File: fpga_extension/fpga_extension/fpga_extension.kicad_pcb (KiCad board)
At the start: 4 copper layers, 50 x 34.7 mm, 78 parts, among them J1 Conn_02x16_Odd_Even, U1 AMS1117-1.2, U2 t20f169, U501 W9825G6KH-6, X1 SG-8101CG, X2 SG-8101CG

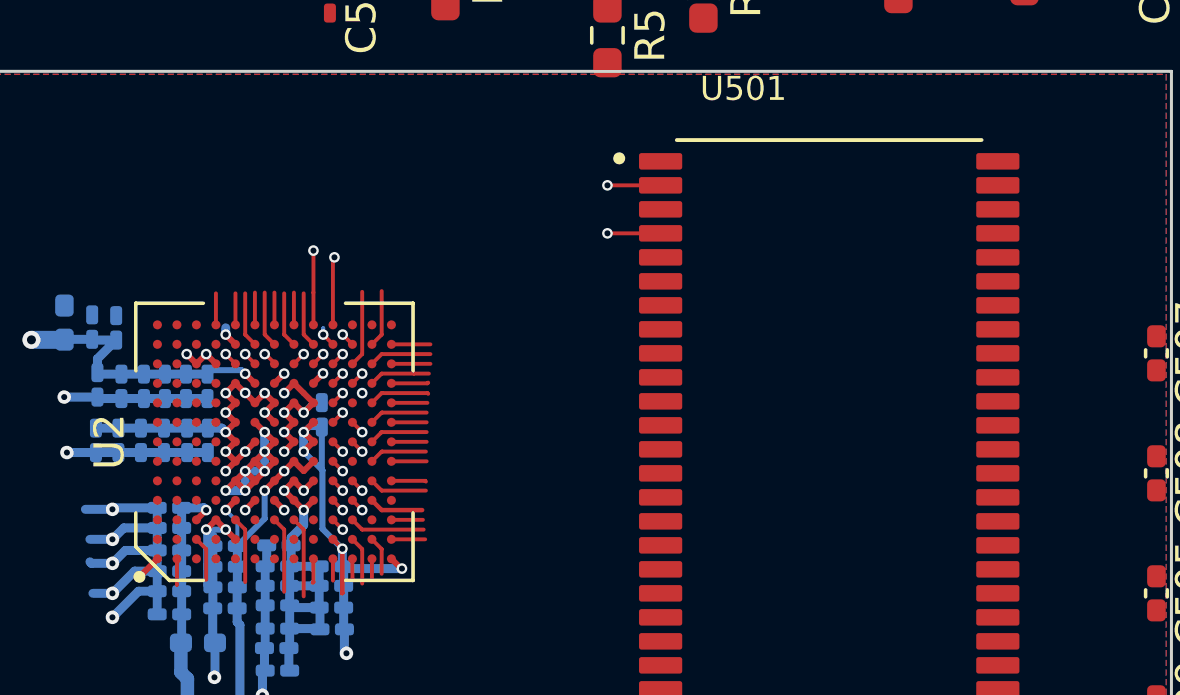
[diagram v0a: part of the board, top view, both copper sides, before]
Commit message: working on new version of fpga extension with Lattice FPGA
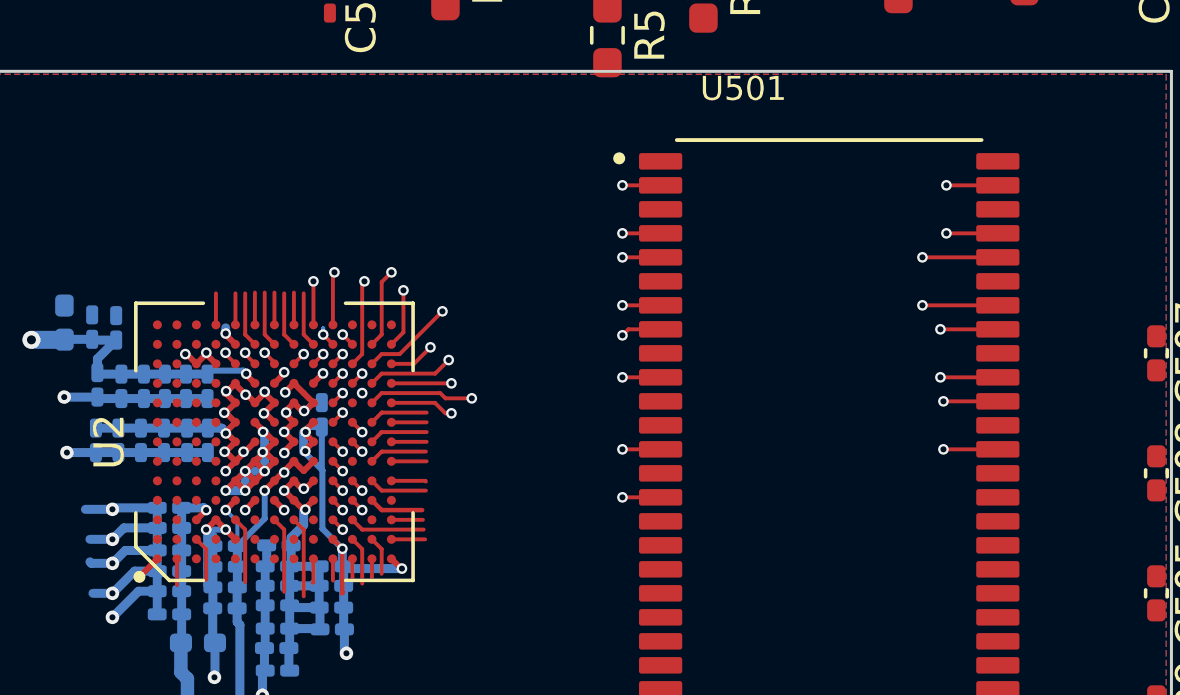
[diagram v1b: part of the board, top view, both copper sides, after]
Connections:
- U2 pad K10: /SDRAM/RAM_D8 -> /SDRAM/RAM_D12
- U2 pad K11: /SDRAM/RAM_D6 -> /SDRAM/RAM_D13
- U2 pad L10: /SDRAM/RAM_CS# -> /SDRAM/RAM_D3
- U2 pad L11: /SDRAM/RAM_RAS# -> /SDRAM/RAM_D15
- U2 pad M10: /SDRAM/RAM_CAS# -> /SDRAM/RAM_D5
- U2 pad M11: /SDRAM/RAM_D5 -> /SDRAM/RAM_D4
- U2 pad M12: /SDRAM/RAM_BS1 -> /SDRAM/RAM_D14
- U2 pad N10: /SDRAM/RAM_D7 -> /SDRAM/RAM_D10
- U2 pad N11: /SDRAM/RAM_D4 -> /SDRAM/RAM_D11
- U2 pad N12: /SDRAM/RAM_BS0 -> /SDRAM/RAM_D2
- U2 pad N2: /SDRAM/RAM_D2 -> /SDRAM/RAM_A3
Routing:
- net /SDRAM/RAM_D14: track 2.56 -> 33.5 mm, vias 1 -> 3
- net /SDRAM/RAM_D3: track 0.00 -> 29.1 mm, vias 0 -> 1
- net /SDRAM/RAM_D2: track 1.12 -> 28.5 mm, vias 0 -> 2
- net /SDRAM/RAM_D4: track 1.30 -> 28.6 mm, vias 0 -> 3
- net /SDRAM/RAM_D5: track 2.08 -> 28.5 mm, vias 0 -> 2
- net /SDRAM/RAM_D15: track 0.00 -> 26.2 mm, vias 0 -> 2
- net /SDRAM/RAM_D13: track 1.18 -> 27.3 mm, vias 0 -> 2
- net /SDRAM/RAM_LDQM: track 3.33 -> 29.4 mm, vias 1 -> 3
- net /SDRAM/RAM_D12: track 2.61 -> 26.8 mm, vias 1 -> 3
- net /SDRAM/RAM_D9: track 2.02 -> 26.1 mm, vias 0 -> 2
- net /SDRAM/RAM_D10: track 3.60 -> 26.1 mm, vias 1 -> 2
- net /SDRAM/RAM_D11: track 1.96 -> 23.8 mm, vias 0 -> 2
- net /SDRAM/RAM_D1: track 14.2 -> 29.1 mm
- net /SDRAM/RAM_D0: track 17.5 -> 31.0 mm
- net /SDRAM/RAM_D8: track 3.68 -> 0.00 mm
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
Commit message: prepared first versions of PCBs
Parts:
- removed C101, C102, C201, C202, C501, C505: 4.7u, Capacitor_SMD:C_0402_1005Metric_Pad0.74x0.62mm_HandSolder
- removed C103, C203, C502, C503, C504: 0.1u, Capacitor_SMD:C_0201_0603Metric_Pad0.64x0.40mm_HandSolder
- removed C506, C507, C508, C509: 0.1u, Capacitor_SMD:C_0402_1005Metric_Pad0.74x0.62mm_HandSolder
- removed L101, L201, L501: 33ohm 100MHz, Inductor_SMD:L_0402_1005Metric_Pad0.77x0.64mm_HandSolder
- removed R101, R201: 33R, Resistor_SMD:R_0603_1608Metric_Pad0.98x0.95mm_HandSolder
- removed R301: 50R, Resistor_SMD:R_0603_1608Metric_Pad0.98x0.95mm_HandSolder
- removed U501: W9825G6KH-6, ram:SOP80P1176X120-54N
- removed X2: SG-8101CG, Oscillator:Oscillator_SMD_SeikoEpson_SG210-4Pin_2.5x2.0mm_HandSoldering
- added C3: 100n, Capacitor_SMD:C_0402_1005Metric_Pad0.74x0.62mm_HandSolder, B.Cu at (159.0, 93.1)
- added C45: 100n, Capacitor_SMD:C_0402_1005Metric_Pad0.74x0.62mm_HandSolder, B.Cu at (152.2, 97.5)
- added C46: 100n, Capacitor_SMD:C_0402_1005Metric_Pad0.74x0.62mm_HandSolder, B.Cu at (155.2, 97.6)
- added C47: 100n, Capacitor_SMD:C_0402_1005Metric_Pad0.74x0.62mm_HandSolder, B.Cu at (148.7, 93.9)
- added C48: 100n, Capacitor_SMD:C_0402_1005Metric_Pad0.74x0.62mm_HandSolder, B.Cu at (148.7, 92.8)
- added C49: 100n, Capacitor_SMD:C_0402_1005Metric_Pad0.74x0.62mm_HandSolder, B.Cu at (148.7, 91.7)
- added C50: 100n, Capacitor_SMD:C_0402_1005Metric_Pad0.74x0.62mm_HandSolder, B.Cu at (154.8, 88.5)
- added C51: 100n, Capacitor_SMD:C_0402_1005Metric_Pad0.74x0.62mm_HandSolder, B.Cu at (152.6, 88.5)
- added C52: 100n, Capacitor_SMD:C_0402_1005Metric_Pad0.74x0.62mm_HandSolder, F.Cu at (180.2, 84.7)
- added C53: 100n, Capacitor_SMD:C_0402_1005Metric_Pad0.74x0.62mm_HandSolder, B.Cu at (159.0, 89.9)
- added C54: 100n, Capacitor_SMD:C_0402_1005Metric_Pad0.74x0.62mm_HandSolder, B.Cu at (159.0, 91.0)
- added C55: 100n, Capacitor_SMD:C_0402_1005Metric_Pad0.74x0.62mm_HandSolder, B.Cu at (158.9, 92.0)
- added C56: 100n, Capacitor_SMD:C_0402_1005Metric_Pad0.74x0.62mm_HandSolder, B.Cu at (150.3, 88.5)
- added C57: 100n, Capacitor_SMD:C_0402_1005Metric_Pad0.74x0.62mm_HandSolder, B.Cu at (149.7, 96.8)
- added C58: 100n, Capacitor_SMD:C_0402_1005Metric_Pad0.74x0.62mm_HandSolder, B.Cu at (157.2, 96.3)
- added C59: 100n, Capacitor_SMD:C_0402_1005Metric_Pad0.74x0.62mm_HandSolder, B.Cu at (155.8, 94.1)
- added C60: 1u, Capacitor_SMD:C_0402_1005Metric_Pad0.74x0.62mm_HandSolder, B.Cu at (159.0, 94.2)
- added C61: 1u, Capacitor_SMD:C_0402_1005Metric_Pad0.74x0.62mm_HandSolder, B.Cu at (146.8, 96.7)
- added C62: 100n, Capacitor_SMD:C_0402_1005Metric_Pad0.74x0.62mm_HandSolder, F.Cu at (183.7, 88.2)
- added D1: D_Schottky, Diode_SMD:D_SOD-323_HandSoldering, B.Cu at (184.6, 116.6)
- added D2: LED, LED_SMD:LED_0402_1005Metric_Pad0.77x0.64mm_HandSolder, F.Cu at (186.0, 99.7)
- added D3: LED, LED_SMD:LED_0402_1005Metric_Pad0.77x0.64mm_HandSolder, F.Cu at (145.1, 110.2)
- added D4: LED, LED_SMD:LED_0402_1005Metric_Pad0.77x0.64mm_HandSolder, F.Cu at (145.1, 109.1)
- added D5: LED, LED_SMD:LED_0402_1005Metric_Pad0.77x0.64mm_HandSolder, F.Cu at (145.1, 108.0)
- added F1: Fuse, Fuse:Fuse_0603_1608Metric_Pad1.05x0.95mm_HandSolder, F.Cu at (175.9, 77.8)
- added FB1: FerriteBead, Inductor_SMD:L_0805_2012Metric_Pad1.05x1.20mm_HandSolder, B.Cu at (174.7, 119.0)
- added FB2: FerriteBead, Inductor_SMD:L_0805_2012Metric_Pad1.05x1.20mm_HandSolder, B.Cu at (142.7, 89.7)
- added FB3: FerriteBead, Inductor_SMD:L_0805_2012Metric_Pad1.05x1.20mm_HandSolder, B.Cu at (165.0, 81.6)
- added J2: Conn_01x03, Connector_PinHeader_2.54mm:PinHeader_1x03_P2.54mm_Vertical, F.Cu at (172.5, 77.9)
- added J3: Micro_SD_Card_Det1, Connector_Card:microSD_HC_Wuerth_693072010801, B.Cu at (150.0, 77.4)
- added J4: Connector A 16-bit, Connector_PinHeader_1.27mm:PinHeader_2x15_P1.27mm_Vertical_SMD, B.Cu at (164.7, 113.5)
- added Q1: TSM2301ACX, Package_TO_SOT_SMD:SOT-23W_Handsoldering, B.Cu at (180.2, 116.8)
- added R10: 4.7k, Resistor_SMD:R_0402_1005Metric_Pad0.72x0.64mm_HandSolder, F.Cu at (155.4, 75.7)
- added R11: DNF, Resistor_SMD:R_0402_1005Metric_Pad0.72x0.64mm_HandSolder, F.Cu at (157.8, 75.7)
- added R12: 4.7k, Resistor_SMD:R_0402_1005Metric_Pad0.72x0.64mm_HandSolder, F.Cu at (155.4, 81.5)
- added R13: 4.7k, Resistor_SMD:R_0402_1005Metric_Pad0.72x0.64mm_HandSolder, F.Cu at (155.4, 74.6)
- added R14: 4.7k, Resistor_SMD:R_0402_1005Metric_Pad0.72x0.64mm_HandSolder, F.Cu at (155.4, 80.4)
- added R15: DNF, Resistor_SMD:R_0402_1005Metric_Pad0.72x0.64mm_HandSolder, F.Cu at (157.8, 74.6)
- added R16: 100k, Resistor_SMD:R_0402_1005Metric_Pad0.72x0.64mm_HandSolder, F.Cu at (184.4, 110.9)
- added R17: 120k, Resistor_SMD:R_0402_1005Metric_Pad0.72x0.64mm_HandSolder, F.Cu at (182.0, 110.9)
- added R18: 10k, Resistor_SMD:R_0402_1005Metric_Pad0.72x0.64mm_HandSolder, B.Cu at (182.1, 114.4)
- added R19: 5.1k, Resistor_SMD:R_0402_1005Metric_Pad0.72x0.64mm_HandSolder, F.Cu at (185.9, 80.4)
- added R20: 5.1k, Resistor_SMD:R_0402_1005Metric_Pad0.72x0.64mm_HandSolder, F.Cu at (181.5, 81.0)
- added R21: 10k, Resistor_SMD:R_0402_1005Metric_Pad0.72x0.64mm_HandSolder, B.Cu at (171.8, 83.2)
- added R22: 27.4, Resistor_SMD:R_0402_1005Metric_Pad0.72x0.64mm_HandSolder, F.Cu at (173.7, 87.1)
- added R23: 27.4, Resistor_SMD:R_0402_1005Metric_Pad0.72x0.64mm_HandSolder, F.Cu at (174.9, 87.1)
- added R24: 1k, Resistor_SMD:R_0402_1005Metric_Pad0.72x0.64mm_HandSolder, F.Cu at (186.6, 94.1)
- added R25: 600, Resistor_SMD:R_0402_1005Metric_Pad0.72x0.64mm_HandSolder, F.Cu at (186.0, 100.9)
- added R26: 10k, Resistor_SMD:R_0402_1005Metric_Pad0.72x0.64mm_HandSolder, F.Cu at (151.8, 74.4)
- added R27: 10k, Resistor_SMD:R_0402_1005Metric_Pad0.72x0.64mm_HandSolder, F.Cu at (146.6, 74.4)
- added R28: <10k, Resistor_SMD:R_0402_1005Metric_Pad0.72x0.64mm_HandSolder, B.Cu at (171.1, 118.6)
- added R29: 600, Resistor_SMD:R_0402_1005Metric_Pad0.72x0.64mm_HandSolder, F.Cu at (147.7, 110.2)
- added R30: 600, Resistor_SMD:R_0402_1005Metric_Pad0.72x0.64mm_HandSolder, F.Cu at (147.7, 109.1)
- added R31: 600, Resistor_SMD:R_0402_1005Metric_Pad0.72x0.64mm_HandSolder, F.Cu at (147.7, 108.0)
- added R32: 22, Resistor_SMD:R_0402_1005Metric_Pad0.72x0.64mm_HandSolder, B.Cu at (143.2, 101.4)
- added R8: 4.7k, Resistor_SMD:R_0402_1005Metric_Pad0.72x0.64mm_HandSolder, F.Cu at (155.4, 79.2)
- added R9: 1k, Resistor_SMD:R_0402_1005Metric_Pad0.72x0.64mm_HandSolder, F.Cu at (155.4, 78.0)
- added U3: W958D8NBYA, footprints:BGA24C100P5X5_600X800X120, F.Cu at (172.2, 98.6)
- added U4: TLV75525PDBV, Package_TO_SOT_SMD:SOT-23-5, F.Cu at (145.2, 115.1)
- added U5: TLV75518PDBV, Package_TO_SOT_SMD:SOT-23-5, F.Cu at (150.6, 115.1)
- added U6: TLV62569DRL, Package_TO_SOT_SMD:SOT-563, F.Cu at (184.9, 108.8)
- added U7: USBLC6-2P6, Package_TO_SOT_SMD:SOT-666, F.Cu at (183.4, 81.5)
- added U8: W25Q128JVS, Package_SO:SOIC-8_5.23x5.23mm_P1.27mm, B.Cu at (168.2, 86.8)
- added U9: RP2040, Package_DFN_QFN:QFN-56-1EP_7x7mm_P0.4mm_EP3.2x3.2mm, B.Cu at (181.9, 87.1)
- added Y1: ECS-120-8-36-CGN-TR, footprints:XTAL_ECS-120-8-36-CGN-TR, F.Cu at (184.5, 94.7)
- C1: value 10u -> 100n; footprint Capacitor_SMD:C_0603_1608Metric_Pad1.08x0.95mm_HandSolder -> Capacitor_SMD:C_0402_1005Metric_Pad0.74x0.62mm_HandSolder; moved to B.Cu
- C10, C11, C12, C13, C9: value 0.1u -> 4.7u; footprint Capacitor_SMD:C_0201_0603Metric_Pad0.64x0.40mm_HandSolder -> Capacitor_SMD:C_0402_1005Metric_Pad0.74x0.62mm_HandSolder; moved to F.Cu
- C14, C15: value 0.1u -> 10u; footprint Capacitor_SMD:C_0201_0603Metric_Pad0.64x0.40mm_HandSolder -> Capacitor_SMD:C_0603_1608Metric_Pad1.08x0.95mm_HandSolder; moved to F.Cu
- C16: value 0.1u -> 6.8p; footprint Capacitor_SMD:C_0201_0603Metric_Pad0.64x0.40mm_HandSolder -> Capacitor_SMD:C_0402_1005Metric_Pad0.74x0.62mm_HandSolder; moved to F.Cu
- C17, C18, C19, C21, C26, C27, C37, C5, C7: value 0.1u -> 100n; footprint Capacitor_SMD:C_0201_0603Metric_Pad0.64x0.40mm_HandSolder -> Capacitor_SMD:C_0402_1005Metric_Pad0.74x0.62mm_HandSolder
- C2: value 10u -> 100n; footprint Capacitor_SMD:C_0603_1608Metric_Pad1.08x0.95mm_HandSolder -> Capacitor_SMD:C_0402_1005Metric_Pad0.74x0.62mm_HandSolder
- C20, C22, C23, C8: value 0.1u -> 4.7u; footprint Capacitor_SMD:C_0201_0603Metric_Pad0.64x0.40mm_HandSolder -> Capacitor_SMD:C_0402_1005Metric_Pad0.74x0.62mm_HandSolder
- C24: footprint Capacitor_SMD:C_0201_0603Metric_Pad0.64x0.40mm_HandSolder -> Capacitor_SMD:C_0402_1005Metric_Pad0.74x0.62mm_HandSolder
- C25, C28: value 0.1u -> 14p; footprint Capacitor_SMD:C_0201_0603Metric_Pad0.64x0.40mm_HandSolder -> Capacitor_SMD:C_0402_1005Metric_Pad0.74x0.62mm_HandSolder; moved to F.Cu
- C29, C32, C34, C36: value 0.1u -> 100n; footprint Capacitor_SMD:C_0201_0603Metric_Pad0.64x0.40mm_HandSolder -> Capacitor_SMD:C_0402_1005Metric_Pad0.74x0.62mm_HandSolder; moved to F.Cu
- C30: value 0.1u -> 1u; footprint Capacitor_SMD:C_0201_0603Metric_Pad0.64x0.40mm_HandSolder -> Capacitor_SMD:C_0402_1005Metric_Pad0.74x0.62mm_HandSolder; moved to F.Cu
- C31, C33, C35, C40: value 0.22u -> 100n; footprint Capacitor_SMD:C_0201_0603Metric_Pad0.64x0.40mm_HandSolder -> Capacitor_SMD:C_0402_1005Metric_Pad0.74x0.62mm_HandSolder; moved to F.Cu
- C38: value 0.22u -> 1u; footprint Capacitor_SMD:C_0201_0603Metric_Pad0.64x0.40mm_HandSolder -> Capacitor_SMD:C_0402_1005Metric_Pad0.74x0.62mm_HandSolder; moved to F.Cu
- C39: value 0.22u -> 10u; footprint Capacitor_SMD:C_0201_0603Metric_Pad0.64x0.40mm_HandSolder -> Capacitor_SMD:C_0402_1005Metric_Pad0.74x0.62mm_HandSolder; moved to F.Cu
- C4: value 4.7u -> 100n
- C41, C43, C44: value 0.22u -> 100n; footprint Capacitor_SMD:C_0201_0603Metric_Pad0.64x0.40mm_HandSolder -> Capacitor_SMD:C_0402_1005Metric_Pad0.74x0.62mm_HandSolder
- C42: value 0.22u -> 4.7u; footprint Capacitor_SMD:C_0201_0603Metric_Pad0.64x0.40mm_HandSolder -> Capacitor_SMD:C_0402_1005Metric_Pad0.74x0.62mm_HandSolder
- J1: value Conn_02x16_Odd_Even -> USB_C_Receptacle_USB2.0_16P; footprint Connector_PinHeader_2.00mm:PinHeader_2x16_P2.00mm_Vertical -> Connector_USB:USB_C_Receptacle_HRO_TYPE-C-31-M-12
- L1: value 33 Ohm 100MHz -> 2.2u; footprint Inductor_SMD:L_0402_1005Metric_Pad0.77x0.64mm_HandSolder -> Inductor_SMD:L_0805_2012Metric_Pad1.15x1.40mm_HandSolder
- R1, R2, R4, R5, R6: value 10k -> 4.7k; footprint Resistor_SMD:R_0603_1608Metric_Pad0.98x0.95mm_HandSolder -> Resistor_SMD:R_0402_1005Metric_Pad0.72x0.64mm_HandSolder
- R3: value 0R -> 4.7k; footprint Resistor_SMD:R_0201_0603Metric_Pad0.64x0.40mm_HandSolder -> Resistor_SMD:R_0402_1005Metric_Pad0.72x0.64mm_HandSolder
- R7: value 10k -> DNF; footprint Resistor_SMD:R_0603_1608Metric_Pad0.98x0.95mm_HandSolder -> Resistor_SMD:R_0402_1005Metric_Pad0.72x0.64mm_HandSolder
- U1: value AMS1117-1.2 -> LFE5UM-85F-7BG381x; footprint Package_TO_SOT_SMD:SOT-223-3_TabPin2 -> Package_BGA:Lattice_caBGA-381_17.0x17.0mm_Layout20x20_P0.8mm_Ball0.4mm_Pad0.4mm_NSMD
- U2: value t20f169 -> W25Q128JVS; footprint CustomBGA:BGA-169_13x13_9.0x9.0mm -> Package_SO:SOIC-8_5.23x5.23mm_P1.27mm
- X1: value SG-8101CG -> SG-8002CE; footprint Oscillator:Oscillator_SMD_SeikoEpson_SG210-4Pin_2.5x2.0mm_HandSoldering -> Oscillator:Oscillator_SMD_SeikoEpson_SG210-4Pin_2.5x2.0mm; moved to B.Cu
- moved L1 80.1 mm to (183.6, 106.1), turned to 180 degrees
- moved C24 69.1 mm to (175.9, 74.9)
- moved C27 60.9 mm to (177.3, 85.9), turned to 90 degrees
- moved J1 58.9 mm to (182.9, 74.2), turned to 180 degrees
- moved C11 54.5 mm to (184.4, 113.2), turned to 180 degrees
- moved R3 54.5 mm to (182.4, 83.8), turned to 180 degrees
- moved C16 53.6 mm to (184.4, 112.1), turned to 180 degrees
- moved C15 51.3 mm to (181.4, 109.6), turned to 180 degrees
- moved C14 48.4 mm to (181.4, 108.0), turned to 180 degrees
- moved R2 47.7 mm to (164.7, 90.4), turned to 180 degrees
- moved C28 44.0 mm to (184.4, 97.0)
- moved C35 43.9 mm to (180.1, 89.3), turned to 0 degrees
- moved C33 43.6 mm to (180.3, 88.1), turned to 0 degrees
- moved C36 43.3 mm to (182.4, 89.3)
- moved C25 41.7 mm to (182.4, 94.0), turned to -90 degrees
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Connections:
- C10 pad 1: +1V2 -> +5V
- C11 pad 1: +3V3 -> +5V
- C12 pad 1: +1V2 -> +2V5
- C13 pad 1: +3V3 -> +1V8
- C14 pad 1: +1V2 -> +1V1
- C15 pad 1: +3V3 -> +1V1
- C16 pad 1: +1V2 -> +1V1
- C16 pad 2: GND -> Net-(U6-FB)
- C17 pad 1: +3V3 -> GND
- C17 pad 2: GND -> +2V5
- C18 pad 1: +1V2 -> Net-(C18-Pad1)
- C19 pad 1: +3V3 -> Net-(C19-Pad1)
- C2 pad 1: +1V2 -> +3V3
- C20 pad 1: +1V2 -> Net-(C18-Pad1)
- C21 pad 1: +3V3 -> Net-(C19-Pad1)
- C22 pad 1: +1V2 -> Net-(C19-Pad1)
- C23 pad 1: +3V3 -> Net-(C19-Pad1)
- C24 pad 1: Net-(C24-Pad1) -> GND
- C24 pad 2: GND -> Net-(U7-VBUS)
- C25 pad 1: +1V2 -> /JTAG/OSC_IN
- C27 pad 1: Net-(C24-Pad1) -> Net-(U9-VREG_VOUT)
- C28 pad 1: +1V2 -> Net-(Y1-OUT/IN)
- C29 pad 1: +3V3 -> Net-(U9-VREG_VOUT)
- C30 pad 1: +1V2 -> Net-(U9-VREG_VOUT)
- C32 pad 1: +1V2 -> +3V3
- C34 pad 1: +1V2 -> +3V3
- C36 pad 1: +1V2 -> +3V3
- C37 pad 1: +1V2 -> +3V3
- C39 pad 1: +1V2 -> +3V3
- C4 pad 1: +3V3 -> +1V8
- C41 pad 1: +1V2 -> +3V3
- C5 pad 1: +3V3 -> +1V8
- C6 pad 1: +1V2 -> +1V8
- C7 pad 1: +3V3 -> +1V8
- C8 pad 1: +1V2 -> +1V8
- C9 pad 1: +3V3 -> +5V
- L1 pad 1: Net-(L1-Pad1) -> Net-(U6-SW)
- L1 pad 2: +1V2 -> +1V1
- R1 pad 1: +3V3 -> /FPGA Configuration/JTAG.TCK
- R1 pad 2: /fpga/CONF_DONE -> GND
- R2 pad 1: Net-(R2-Pad1) -> +3V3
- R2 pad 2: GND -> /FPGA Configuration/CFG.CSS
- R3 pad 1: Net-(L1-Pad1) -> +3V3
- R3 pad 2: Net-(C24-Pad1) -> /FPGA Configuration/JTAG.TDI
- R4 pad 1: /fpga/CONF_RESET -> +3V3
- R4 pad 2: GND -> /FPGA Configuration/JTAG.TDO
- R5 pad 2: Net-(R5-Pad2) -> /FPGA Configuration/JTAG.TMS
- R6 pad 2: Net-(R6-Pad2) -> /FPGA Configuration/CFG.CFG2
- R7 pad 1: +3V3 -> /FPGA Configuration/CFG.CFG2
- R7 pad 2: Net-(R7-Pad2) -> GND
- X1 pad 1: Net-(C102-Pad1) -> +3V3
- X1 pad 4: Net-(C102-Pad1) -> +3V3
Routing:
- net +3V3: track 106.8 -> 215.9 mm, vias 13 -> 31
- net +1V1: track 0.00 -> 75.2 mm, vias 0 -> 6
- net +5V: track 0.00 -> 62.4 mm, vias 0 -> 9
- net /Connector/BUS.D3: track 0.00 -> 57.2 mm, vias 0 -> 3
- net /Connector/BUS.D5: track 0.00 -> 56.8 mm, vias 0 -> 3
- net +1V8: track 0.00 -> 56.6 mm, vias 0 -> 9
- net /Connector/BUS.D4: track 0.00 -> 56.4 mm, vias 0 -> 2
- net /Connector/BUS.D7: track 0.00 -> 56.1 mm, vias 0 -> 3
- net /Connector/BUS.D0: track 0.00 -> 56.1 mm, vias 0 -> 2
- net /Connector/BUS.D8: track 0.00 -> 55.9 mm, vias 0 -> 2
- net /Connector/BUS.CLK: track 0.00 -> 55.8 mm, vias 0 -> 3
- net /Connector/BUS.D1: track 0.00 -> 55.2 mm, vias 0 -> 3
- net /Connector/BUS.D2: track 0.00 -> 55.2 mm, vias 0 -> 2
- net /FPGA Configuration/CFG.CFG1: track 0.00 -> 54.2 mm, vias 0 -> 2
- net /Connector/BUS.D6: track 0.00 -> 54.2 mm, vias 0 -> 2
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- added copper zone on B.Cu, net +5V
- added copper zone on In1.Cu, net GND
- added copper zone on In4.Cu, net GND
- removed copper zone on B.Cu, net GND
- removed copper zone on F.Cu, net GND
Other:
- board size 50 x 34.7 mm -> 47.5 x 50 mm
- copper layers 4 -> 6
- rule pad_to_mask_clearance: 0.1016 -> 0
- board text added: "MSPCv2 FPGA ECP5"
- board text added: "Mateusz Stadnik (2024)"
